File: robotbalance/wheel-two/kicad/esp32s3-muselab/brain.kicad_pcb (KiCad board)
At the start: 2 copper layers, 134.6 x 58.4 mm, 0 parts

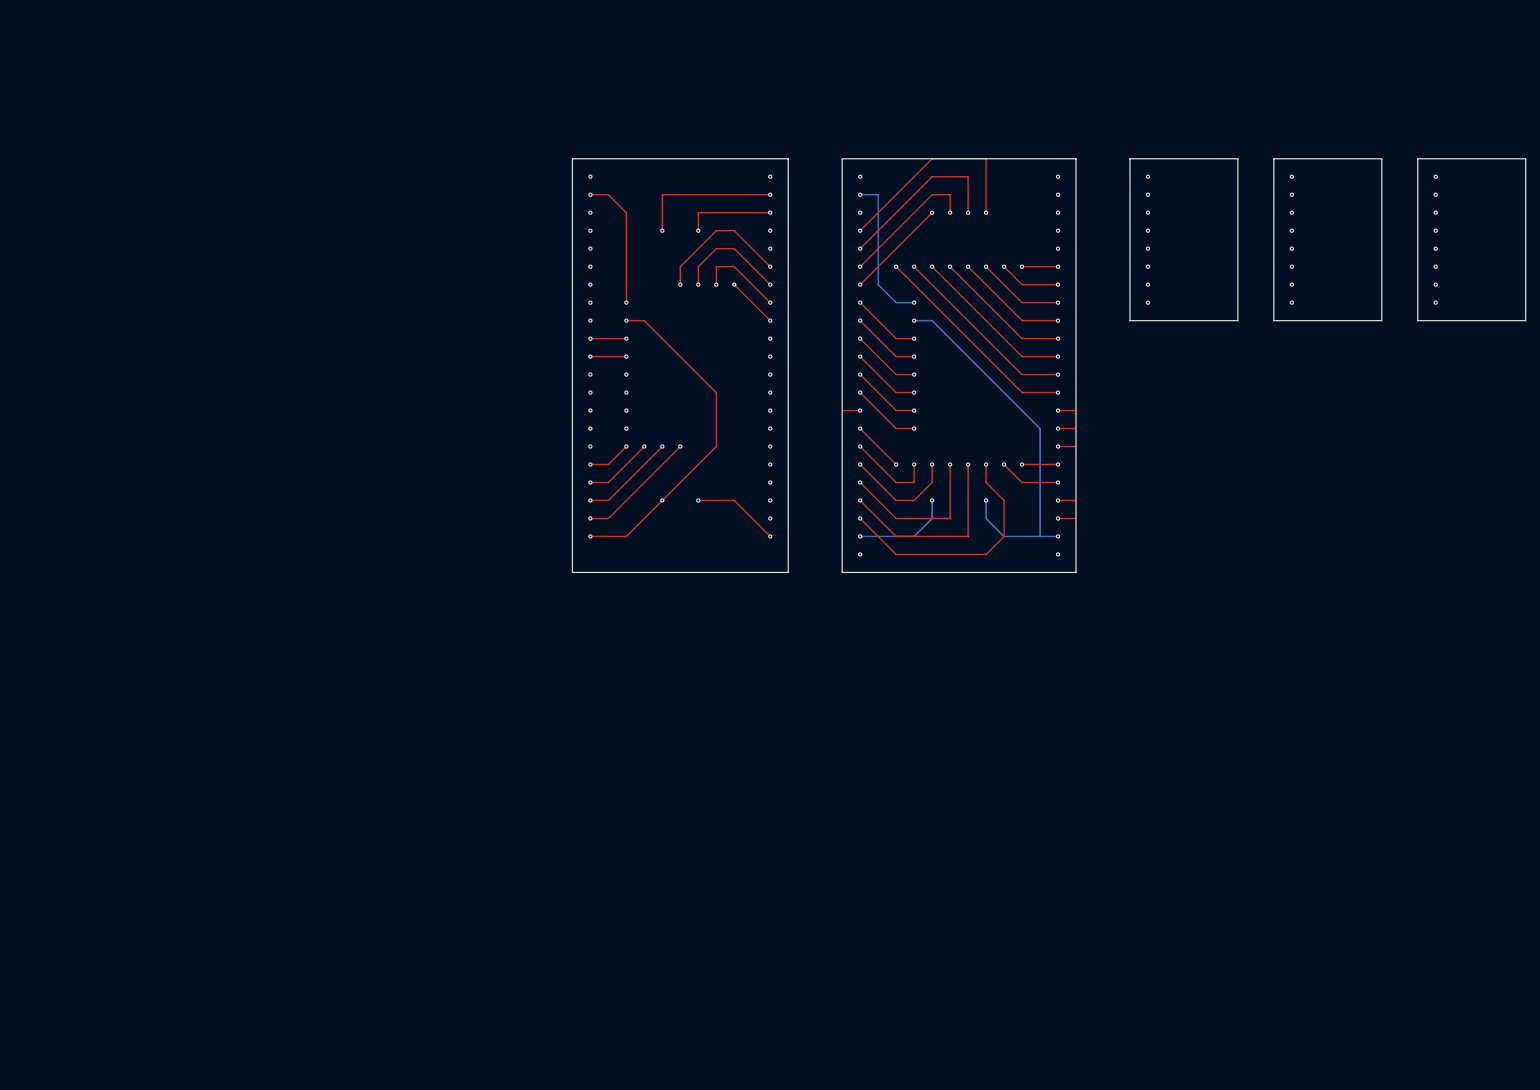
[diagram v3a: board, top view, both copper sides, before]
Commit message: esp32s3 arduino: udp, bmi270, mpu9250
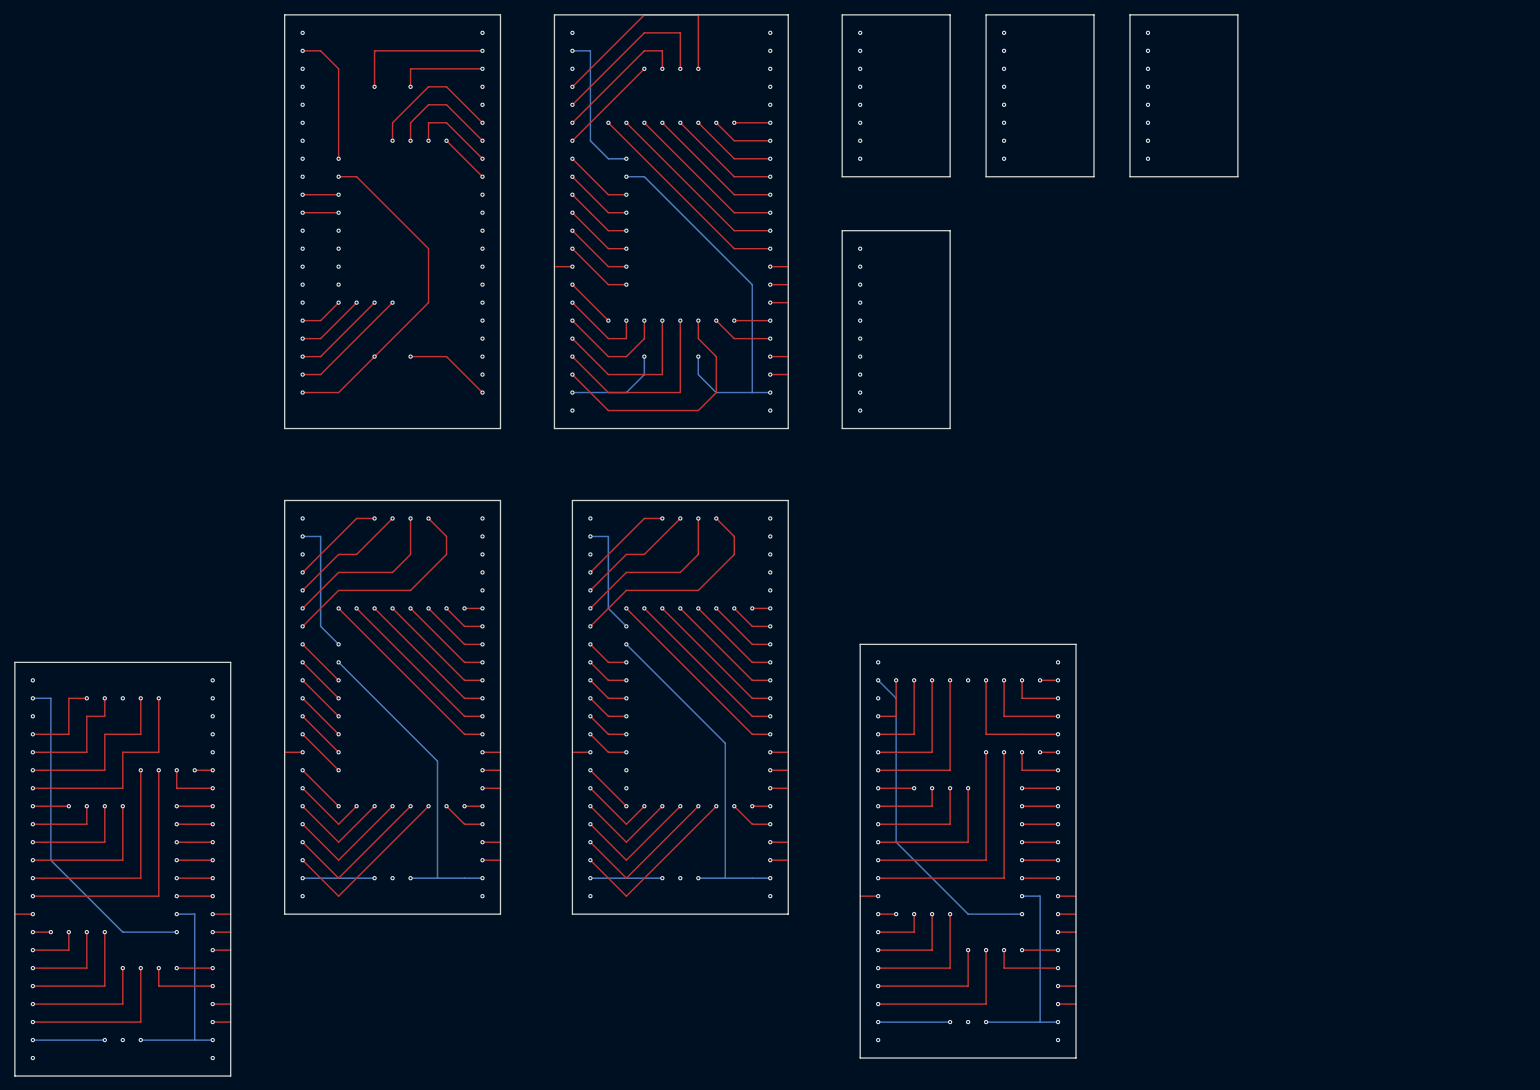
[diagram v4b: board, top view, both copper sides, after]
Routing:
- net (no net): track 747.3 -> 2531.4 mm, vias 160 -> 478
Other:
- board size 134.6 x 58.4 mm -> 172.7 x 149.9 mm
- board text added: "ecl"
- board text added: "eda"
- board text added: "esp32_telesky(vcc-gnd(2022-v1.3))"
- board text added: "esp32_telesky(vcc-gnd(2022-v1.3)) failed: hard to solder on hole board"
- board text added: "esp32s3_vcc-gnd(type-a-v1.5)"
- board text added: "esp32s3_vcc-gnd(type-a-v1.5) fail: hard to solder on hole board!"
- board text added: "fsync"
- board text added: "mpu9250"
- board text added: "ncs"

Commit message: battery/xxx, 6 leg robot, balancing robot, esp32-can
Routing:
- net (no net): track 2531.4 -> 2560.4 mm, vias 478 -> 484
